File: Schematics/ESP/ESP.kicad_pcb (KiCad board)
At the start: 2 copper layers, 66 parts, among them J1 Barrel_Jack, J10 Conn_01x03_Socket, J11 Conn_01x02_Pin, J12 Conn_01x02_Pin, J13 Conn_01x02_Pin, J14 Conn_02x19_Odd_Even, J16 Conn_02x19_Odd_Even, J2 Conn_01x06_Pin, J3 Conn_01x04_Pin, J4 Conn_01x02_Male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

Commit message: PCB layout done no wiring
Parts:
- removed J7: Conn_01x07_Pin, Connector_PinSocket_2.54mm:PinSocket_1x07_P2.54mm_Vertical
- removed R15, R18: 2k, Resistor_SMD:R_1206_3216Metric_Pad1.30x1.75mm_HandSolder
- added C12: 10n, Capacitor_SMD:C_1206_3216Metric_Pad1.33x1.80mm_HandSolder, F.Cu at (91.4, 145.4)
- added C13: 680u, Capacitor_THT:CP_Radial_D10.0mm_P5.00mm, F.Cu at (106.1, 169.4)
- added C14: 10n, Capacitor_SMD:C_1206_3216Metric_Pad1.33x1.80mm_HandSolder, F.Cu at (80.1, 92.6)
- added C15: 10n, Capacitor_SMD:C_1206_3216Metric_Pad1.33x1.80mm_HandSolder, F.Cu at (91.2, 114.0)
- added D5: 1N4001, Diode_THT:D_DO-41_SOD81_P10.16mm_Horizontal, F.Cu at (101.6, 159.8)
- added J8: BLE, Connector_PinSocket_2.54mm:PinSocket_1x06_P2.54mm_Vertical, F.Cu at (98.2, 145.6)
- added R21: 3k3, Resistor_SMD:R_1206_3216Metric_Pad1.30x1.75mm_HandSolder, F.Cu at (85.3, 82.8)
- added R3k1: 3k3, Resistor_SMD:R_1206_3216Metric_Pad1.30x1.75mm_HandSolder, F.Cu at (86.8, 121.4)
- J10: value Conn_01x03_Socket -> IR 2; footprint Connector_PinHeader_1.00mm:PinHeader_1x03_P1.00mm_Vertical -> Connector_PinHeader_2.54mm:PinHeader_1x03_P2.54mm_Vertical
- J11: value Conn_01x02_Pin -> Bumper 1; footprint Connector_PinSocket_1.00mm:PinSocket_1x02_P1.00mm_Vertical -> Connector_PinSocket_2.54mm:PinSocket_1x02_P2.54mm_Vertical
- J12: value Conn_01x02_Pin -> Bumper 2; footprint Connector_PinSocket_1.00mm:PinSocket_1x02_P1.00mm_Vertical -> Connector_PinSocket_2.54mm:PinSocket_1x02_P2.54mm_Vertical
- J13: value Conn_01x02_Pin -> Battery Input
- J2: value Conn_01x06_Pin -> IMU; footprint Connector_PinSocket_2.54mm:PinSocket_1x06_P2.54mm_Vertical -> Connector_PinSocket_2.54mm:PinSocket_1x07_P2.54mm_Vertical
- J3: value Conn_01x04_Pin -> Battery charger
- J4: value Conn_01x02_Male -> Motor A; footprint Connector_PinHeader_1.27mm:PinHeader_1x02_P1.27mm_Horizontal -> Connector_PinHeader_2.54mm:PinHeader_1x02_P2.54mm_Horizontal
- J5: value Conn_01x02_Male -> Motor B; footprint Connector_PinHeader_1.27mm:PinHeader_1x02_P1.27mm_Horizontal -> Connector_PinHeader_2.54mm:PinHeader_1x02_P2.54mm_Horizontal
- J6: value Screw_Terminal_01x02 Fan -> Fan
- J9: value Conn_01x03_Socket -> IR 1; footprint Connector_PinHeader_1.00mm:PinHeader_1x03_P1.00mm_Vertical -> Connector_PinHeader_2.54mm:PinHeader_1x03_P2.54mm_Vertical
- Q17: value IRF540N -> PJP18N20
- R13: value 10k -> 6.2k
- moved J6 101.2 mm to (96.1, 169.4), turned to 180 degrees
- moved J11 96.3 mm to (118.3, 68.0)
- moved F4 76.5 mm to (76.9, 160.1)
- moved J9 76.5 mm to (80.1, 64.9), turned to -90 degrees
- moved J10 68.8 mm to (64.9, 72.5), turned to 0 degrees
- moved Q17 64.3 mm to (78.1, 152.6), turned to 180 degrees
- moved D4 63.2 mm to (83.9, 151.3), turned to 0 degrees
- moved R14 62.9 mm to (100.0, 155.5), turned to 180 degrees
- moved J16 61.6 mm to (120.9, 136.2), turned to 90 degrees
- moved R10 61.2 mm to (76.4, 147.9), turned to 180 degrees
- moved R8 60.9 mm to (83.8, 148.6), turned to 180 degrees
- moved J2 60.5 mm to (123.1, 128.7), turned to -90 degrees
- moved R12 60.0 mm to (95.3, 153.9), turned to 90 degrees
- moved R13 55.1 mm to (91.3, 148.7), turned to 180 degrees
- moved J4 52.2 mm to (112.2, 112.9), turned to 0 degrees
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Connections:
- C7 pad 1: Net-(Q15-S) -> Battery+
- F1 pad 1: Battery+ -> +12V
- J14 pad 1: unconnected-(J14-Pin_1-Pad1) -> Bumper Button 1
- J14 pad 17: unconnected-(J14-Pin_17-Pad17) -> Bumper Button 2
- J14 pad 21: Net-(J14-Pin_21) -> unconnected-(J14-Pin_21-Pad21)
- J14 pad 30: unconnected-(J14-Pin_30-Pad30) -> InputB2
- J14 pad 34: unconnected-(J14-Pin_34-Pad34) -> InputB1
- J16 pad 12: unconnected-(J16-Pin_12-Pad12) -> Net-(J16-Pin_12)
- J16 pad 13: InputA1 -> unconnected-(J16-Pin_13-Pad13)
- J16 pad 14: Fan Signal -> Net-(J16-Pin_14)
- J16 pad 17: InputB1 -> unconnected-(J16-Pin_17-Pad17)
- J16 pad 21: Net-(J16-Pin_21) -> unconnected-(J16-Pin_21-Pad21)
- J16 pad 24: unconnected-(J16-Pin_24-Pad24) -> Battery level
- J16 pad 25: unconnected-(J16-Pin_25-Pad25) -> InputA1
- J16 pad 29: unconnected-(J16-Pin_29-Pad29) -> InputA2
- J16 pad 30: unconnected-(J16-Pin_30-Pad30) -> Fan Signal
- J16 pad 33: Net-(J16-Pin_33) -> unconnected-(J16-Pin_33-Pad33)
- J16 pad 34: Bumper Button 2 -> unconnected-(J16-Pin_34-Pad34)
- J16 pad 4: Bumper Button 1 -> unconnected-(J16-Pin_4-Pad4)
- J16 pad 5: unconnected-(J16-Pin_5-Pad5) -> Net-(J16-Pin_5)
- J16 pad 6: Battery level -> unconnected-(J16-Pin_6-Pad6)
- J16 pad 7: Battery- -> unconnected-(J16-Pin_7-Pad7)
- J16 pad 9: unconnected-(J16-Pin_9-Pad9) -> Battery-
- J2 pad 1: unconnected-(J2-Pin_1-Pad1) -> +5V
- J2 pad 2: Net-(J16-Pin_21) -> Battery-
- J2 pad 3: Net-(J16-Pin_33) -> Net-(J16-Pin_3)
- J2 pad 4: Battery- -> Net-(J16-Pin_5)
- J2 pad 5: +5V -> unconnected-(J2-Pin_5-Pad5)
- J4 pad 1: MotorA+ -> unconnected-(J4-Pin_1-Pad1)
- J4 pad 2: MotorA- -> MotorA+
- J5 pad 1: MotorB+ -> MotorB-
- J5 pad 2: MotorB- -> MotorB+
- Q15 pad 2: Net-(Q15-S) -> Battery+
- R1 pad 2: Net-(J16-Pin_3) -> Net-(J16-Pin_5)
- R7 pad 2: Net-(J14-Pin_21) -> Net-(J16-Pin_3)
- U5 pad 1: Net-(Q15-S) -> Battery+
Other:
- board text removed: "BLE"
- board text removed: "Battery Monitor"
- board text removed: "Bumper 1"
- board text removed: "Bumper 2"
- board text removed: "FAN"
- board text removed: "IR 2"
- board text removed: "MPU"
- board text removed: "Motor A"
- board text removed: "Motor B"

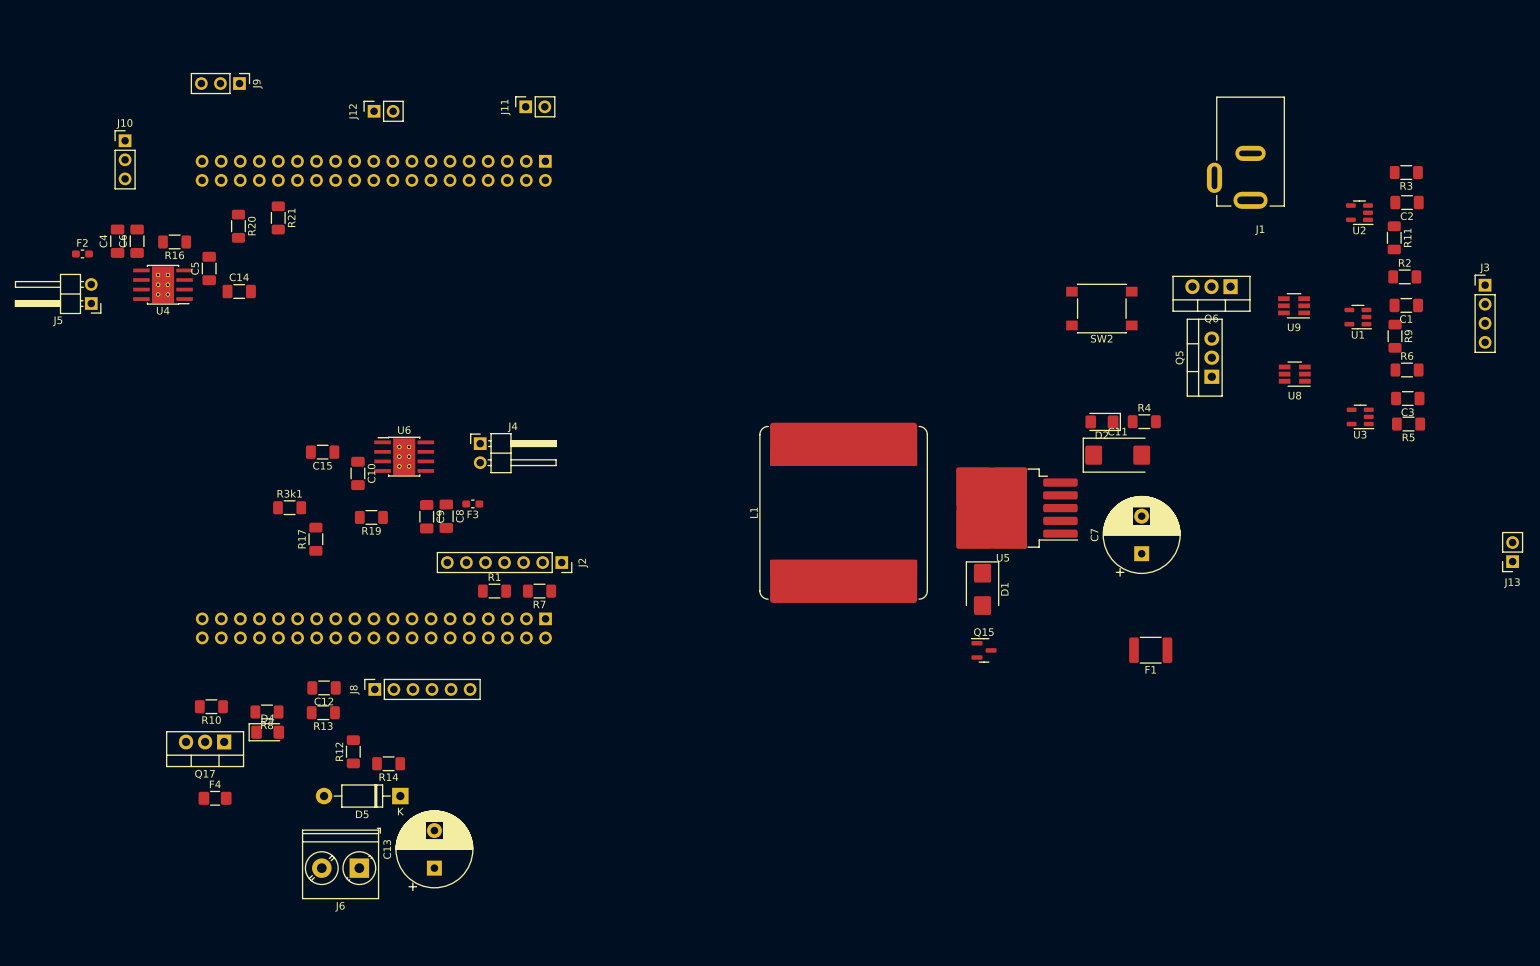
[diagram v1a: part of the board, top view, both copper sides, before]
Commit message: PCB layout done no wiring
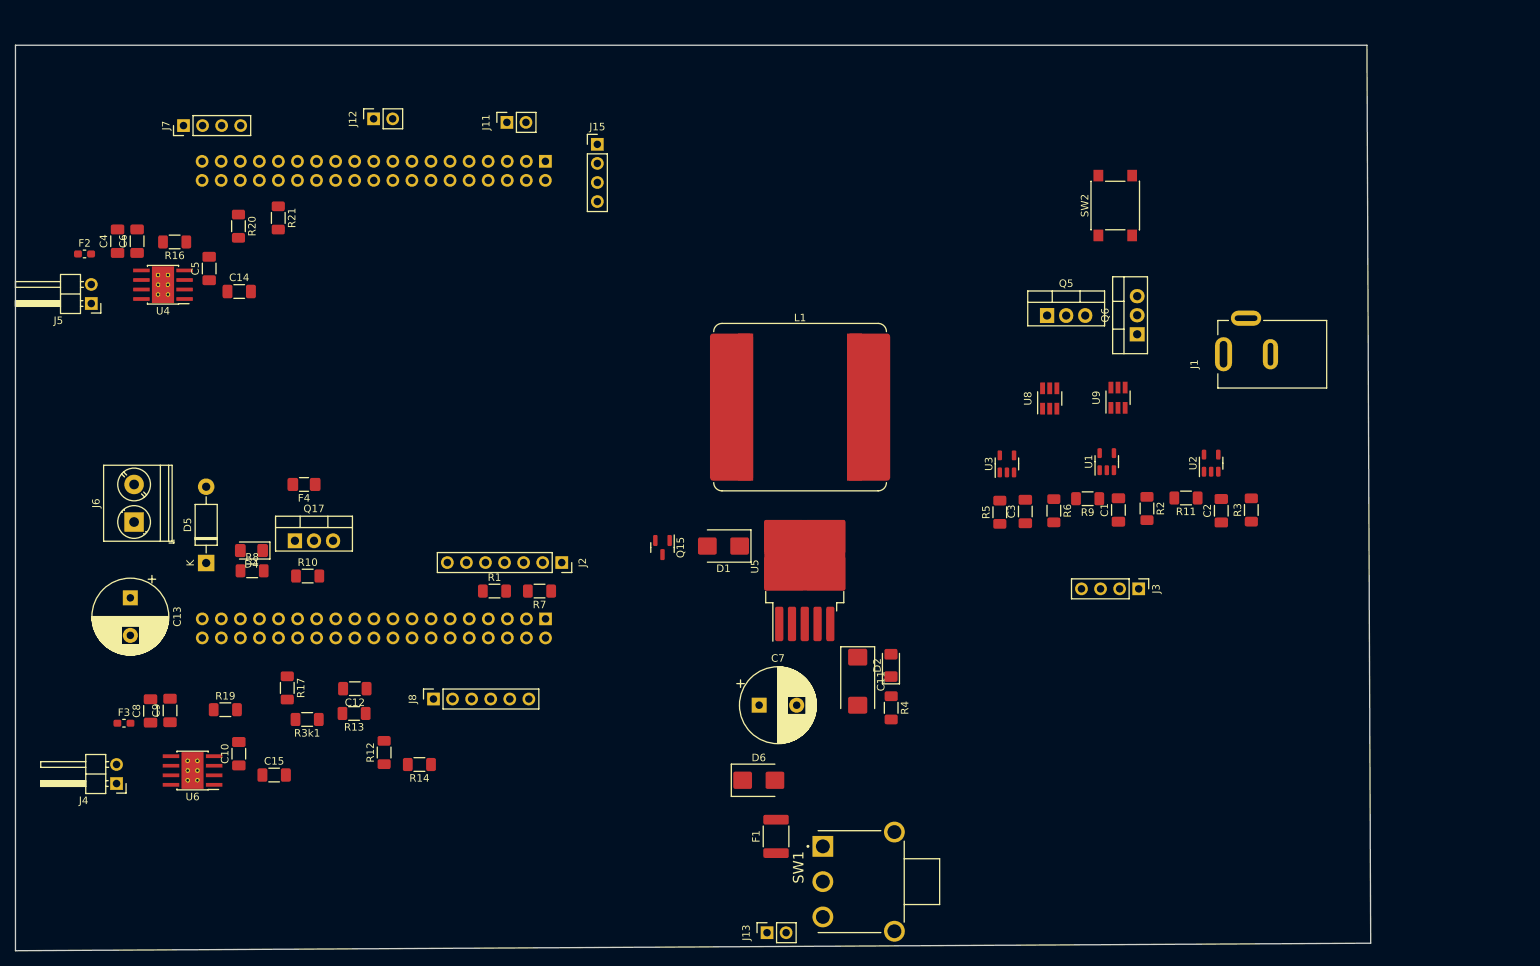
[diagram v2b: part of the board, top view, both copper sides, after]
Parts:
- removed J10: IR 2, Connector_PinHeader_2.54mm:PinHeader_1x03_P2.54mm_Vertical
- removed J9: IR 1, Connector_PinHeader_2.54mm:PinHeader_1x03_P2.54mm_Vertical
- added D6: PMEG045V050EPDZ, Diode_SMD:D_SMB, F.Cu at (149.3, 157.7)
- added J15: UltraSconic B, Connector_PinHeader_2.54mm:PinHeader_1x04_P2.54mm_Vertical, F.Cu at (127.8, 73.0)
- added J7: UltraSonic A, Connector_PinHeader_2.54mm:PinHeader_1x04_P2.54mm_Vertical, F.Cu at (72.7, 70.5)
- added SW1: SW_SPDT, 500SSP1S1M6QEA:SW_500SSP1S1M6QEA, F.Cu at (162.6, 171.2)
- moved J13 110.9 mm to (150.4, 178.0), turned to 90 degrees
- moved J4 66.3 mm to (63.8, 158.1), turned to 180 degrees
- moved J3 61.4 mm to (199.9, 132.2), turned to -90 degrees
- moved F1 55.7 mm to (151.6, 165.2), turned to 90 degrees
- moved R5 55.7 mm to (181.4, 122.0), turned to 90 degrees
- moved J6 55.0 mm to (66.1, 123.3), turned to 90 degrees
- moved F3 54.9 mm to (64.8, 150.1), turned to 0 degrees
- moved C7 54.8 mm to (149.3, 147.7), turned to 0 degrees
- moved C13 54.2 mm to (65.6, 133.4), turned to -90 degrees
- moved C3 53.1 mm to (184.8, 121.9), turned to 90 degrees
- moved R4 50.9 mm to (166.9, 148.1), turned to -90 degrees
- moved R6 50.6 mm to (188.6, 121.8), turned to -90 degrees
- moved U6 50.4 mm to (73.9, 156.4), turned to 180 degrees
- moved R3 49.5 mm to (214.9, 121.7), turned to 90 degrees
- moved C2 47.9 mm to (210.9, 121.8), turned to 90 degrees
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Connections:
- C13 pad 1: Battery+ -> +12V
- C7 pad 1: Battery+ -> +12V
- D5 pad 1: Battery+ -> +12V
- F1 pad 1: +12V -> Net-(SW1-A)
- F1 pad 2: Net-(Q15-D) -> Net-(D6-A)
- F2 pad 1: Battery+ -> +12V
- F3 pad 1: Battery+ -> +12V
- J14 pad 1: Bumper Button 1 -> Echo B
- J14 pad 2: unconnected-(J14-Pin_2-Pad2) -> Trig B
- J14 pad 3: unconnected-(J14-Pin_3-Pad3) -> Bumper Button 1
- J14 pad 35: Motion Sensor A -> Trig A
- J14 pad 37: Motion Sensor B -> Echo A
- J16 pad 25: InputA1 -> unconnected-(J16-Pin_25-Pad25)
- J16 pad 26: unconnected-(J16-Pin_26-Pad26) -> InputA2
- J16 pad 28: unconnected-(J16-Pin_28-Pad28) -> InputA1
- J16 pad 29: InputA2 -> unconnected-(J16-Pin_29-Pad29)
- J16 pad 30: Fan Signal -> unconnected-(J16-Pin_30-Pad30)
- J16 pad 33: unconnected-(J16-Pin_33-Pad33) -> Fan Signal
- J4 pad 1: unconnected-(J4-Pin_1-Pad1) -> MotorA-
- J6 pad 1: Battery+ -> +12V
- R14 pad 1: Battery+ -> +12V
- U5 pad 1: Battery+ -> +12V
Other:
- board outline added: 180.5 x 120.6 mm

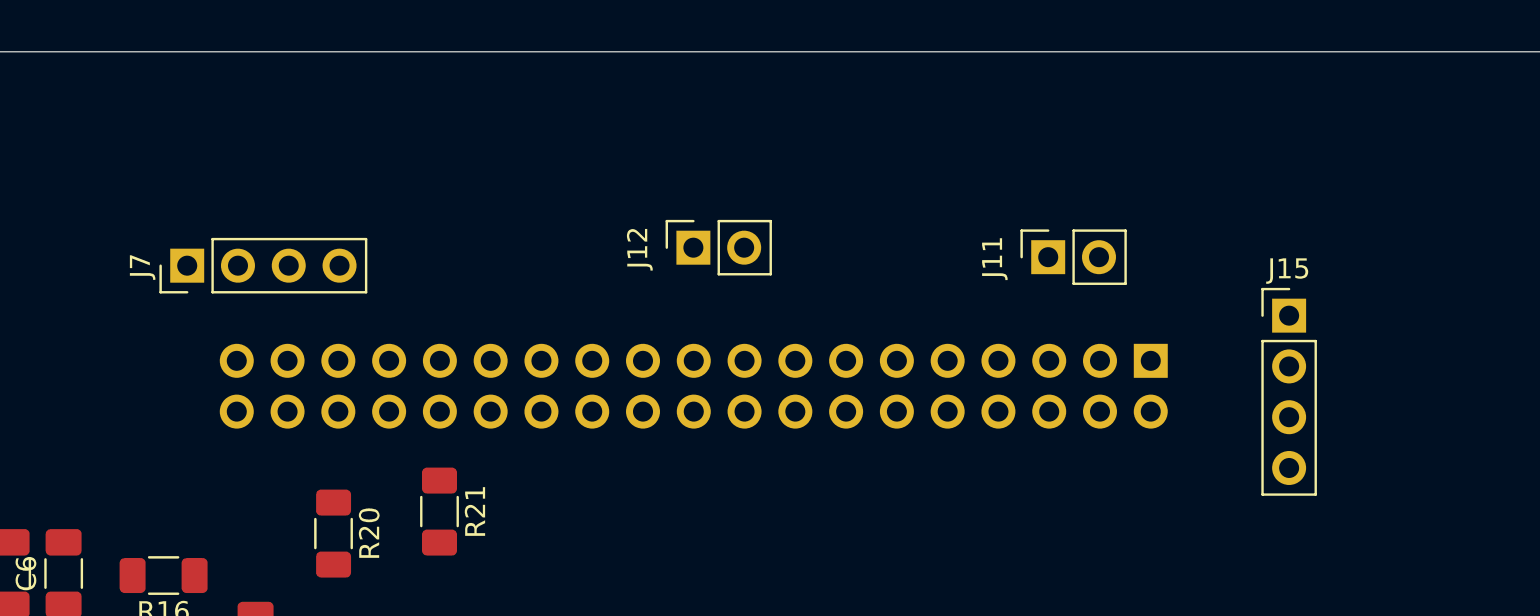
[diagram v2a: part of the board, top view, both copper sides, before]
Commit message: PCB layout done no wiring
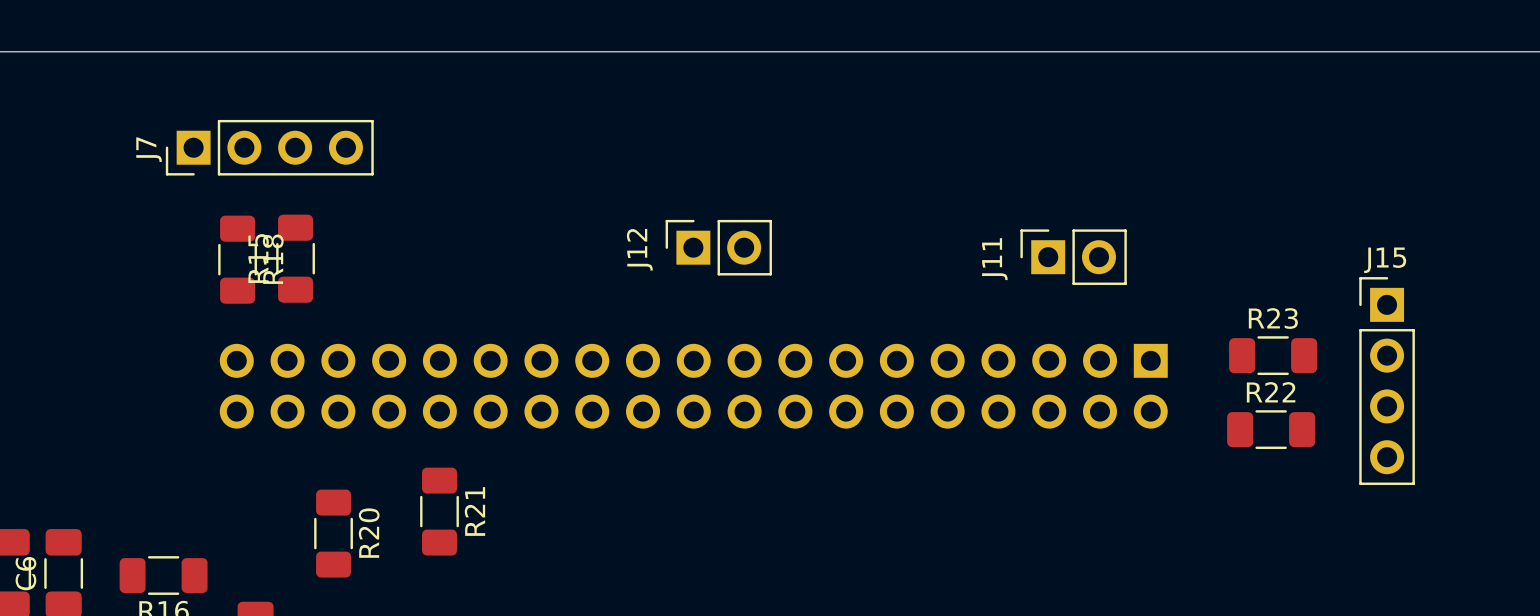
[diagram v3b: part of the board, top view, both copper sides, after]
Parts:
- added R15: 10k, Resistor_SMD:R_1206_3216Metric_Pad1.30x1.75mm_HandSolder, F.Cu at (78.1, 70.2)
- added R18: 10k, Resistor_SMD:R_1206_3216Metric_Pad1.30x1.75mm_HandSolder, F.Cu at (75.2, 70.2)
- added R22: 10k, Resistor_SMD:R_1206_3216Metric_Pad1.30x1.75mm_HandSolder, F.Cu at (126.9, 78.7)
- added R23: 10k, Resistor_SMD:R_1206_3216Metric_Pad1.30x1.75mm_HandSolder, F.Cu at (127.0, 75.0)
- moved J7 5.91 mm to (73.0, 64.6)
- moved J15 4.93 mm to (132.7, 72.5)
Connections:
- J15 pad 2: Echo B -> Net-(J15-Pin_2)
- J15 pad 3: Trig B -> Net-(J15-Pin_3)
- J7 pad 2: Echo A -> Net-(J7-Pin_2)
- J7 pad 3: Trig A -> Net-(J7-Pin_3)
